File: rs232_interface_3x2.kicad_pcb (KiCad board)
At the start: 2 copper layers, 69.8 x 40.6 mm, 1 part

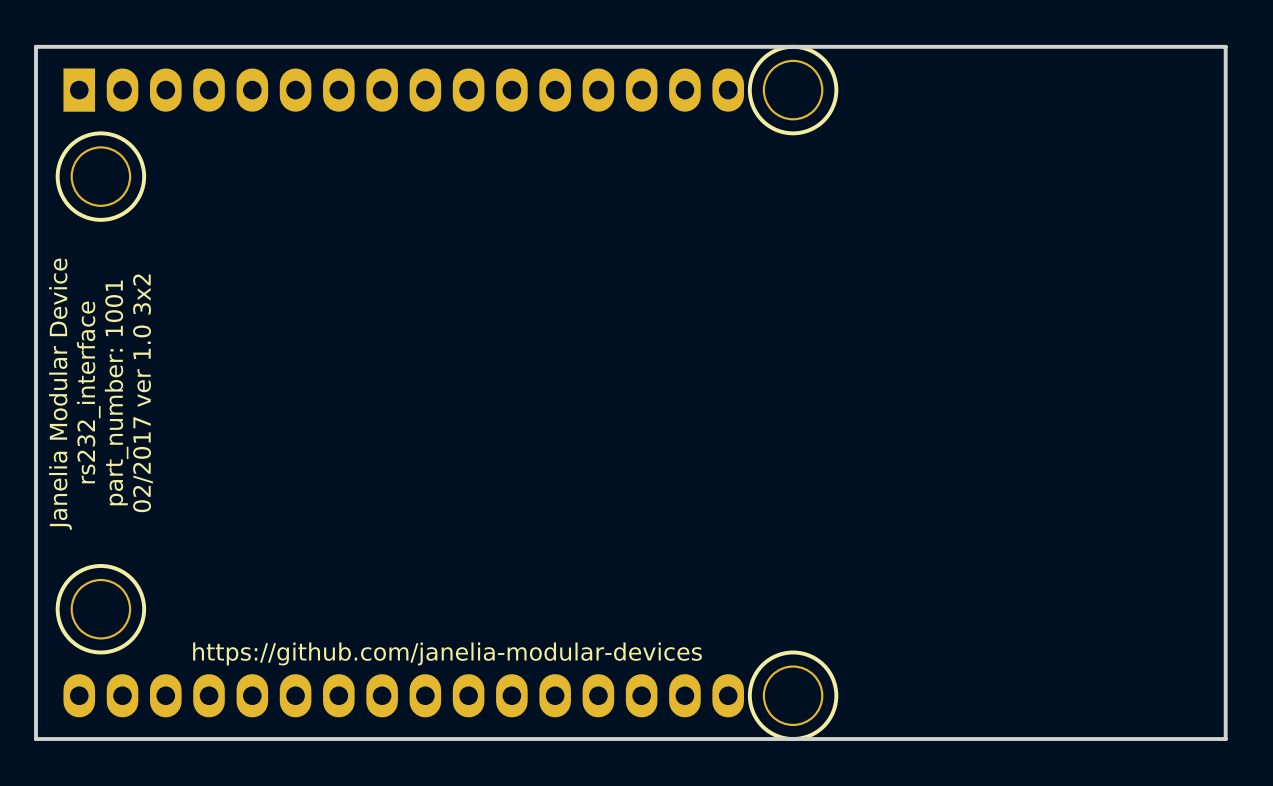
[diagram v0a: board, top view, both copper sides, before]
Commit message: Updated edge positions.
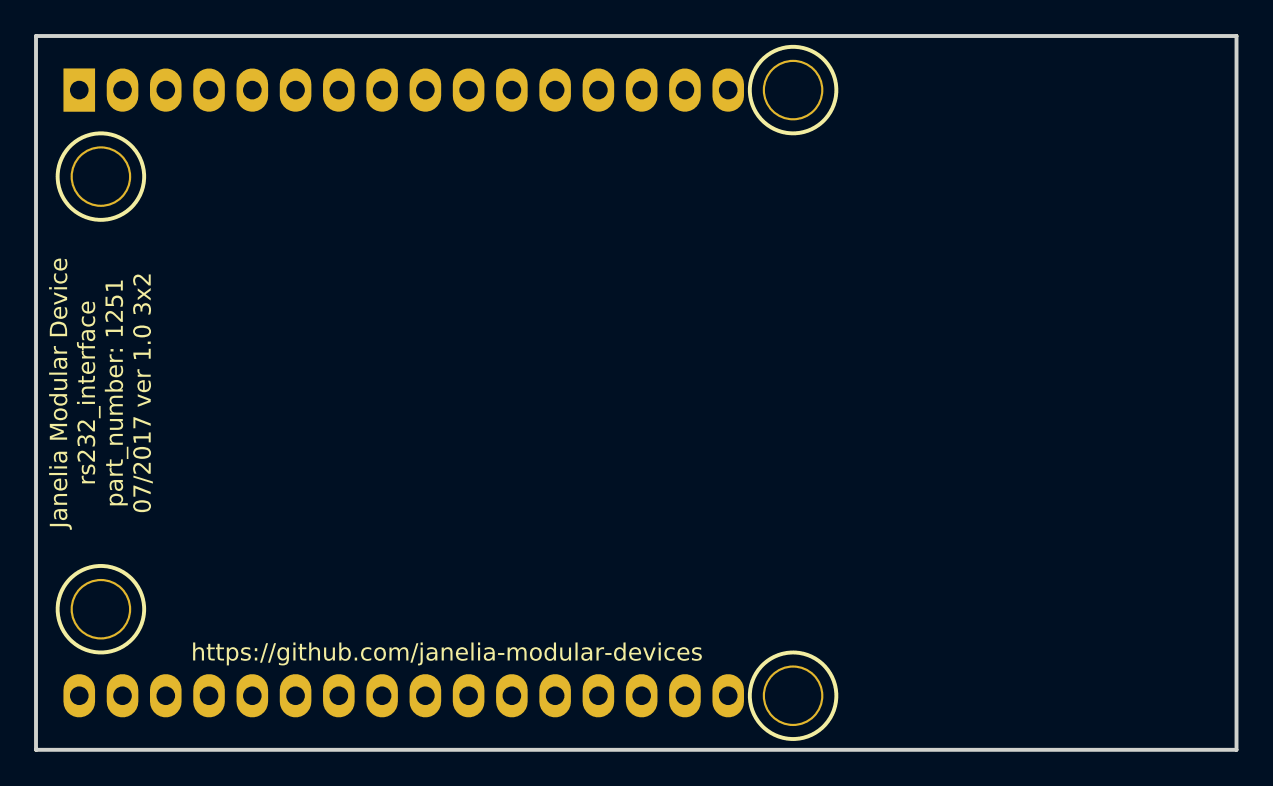
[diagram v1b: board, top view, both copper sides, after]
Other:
- board size 69.8 x 40.6 mm -> 70.5 x 41.9 mm
- board text added: "Janelia Modular Device rs232_interface part_number: 1251 07/2017 ver 1.0 3x2"
- board text removed: "Janelia Modular Device rs232_interface part_number: 1001 02/2017 ver 1.0 3x2"
